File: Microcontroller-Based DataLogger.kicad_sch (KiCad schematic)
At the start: 25 parts, among them U1 24LC1025, U2 24LC1025, U3 DS1337S+, U4 ATMEGA328P-AN, Y1 Crystal, Y2 Crystal

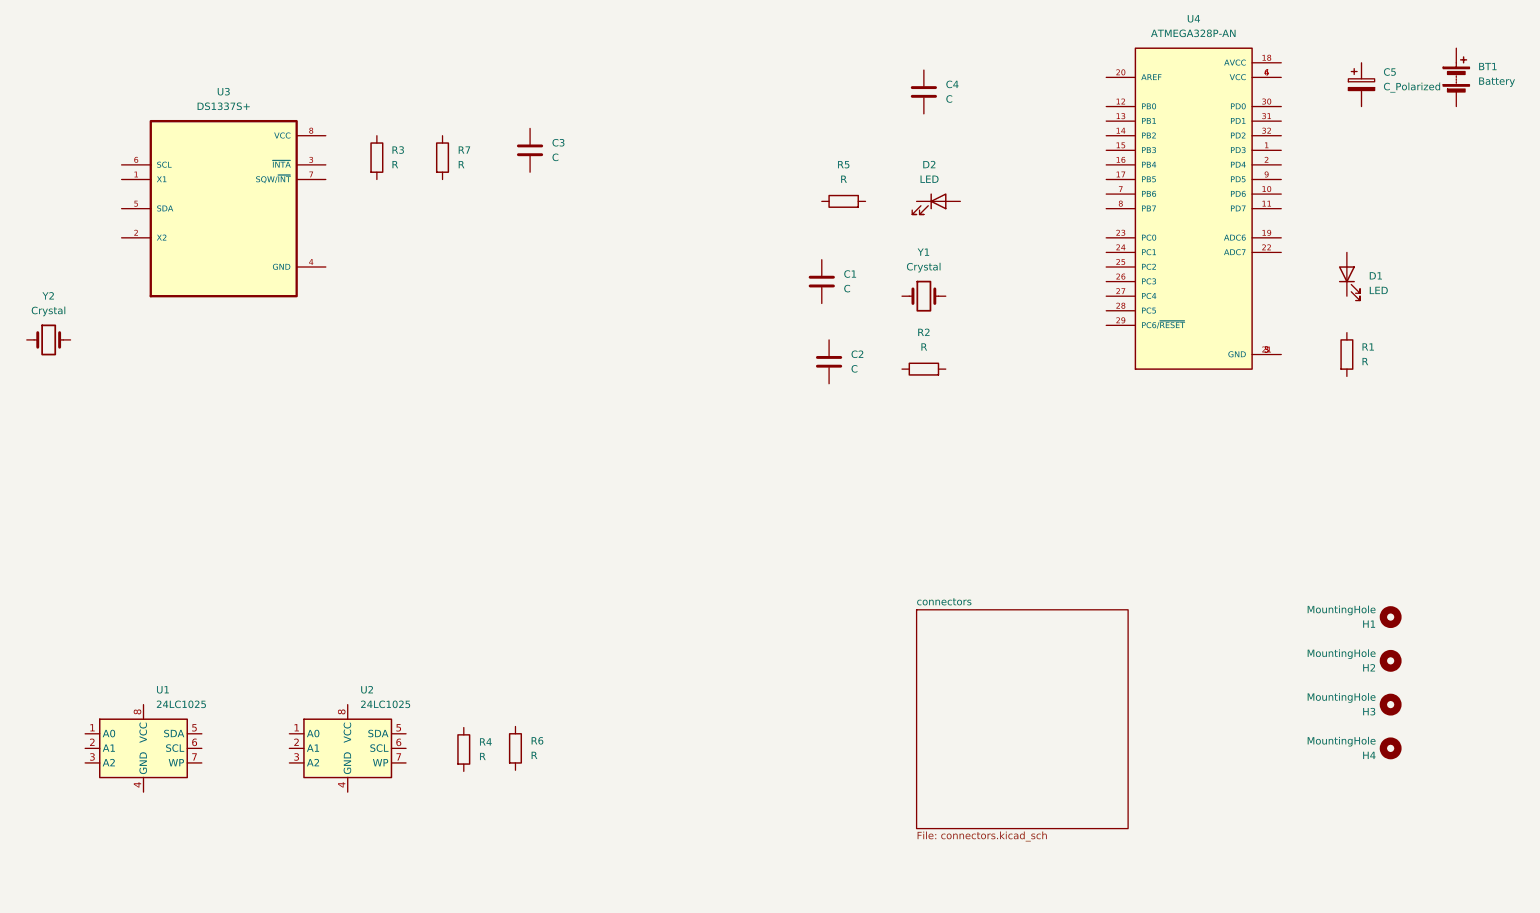
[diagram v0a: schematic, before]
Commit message: Completed symbol footprints.
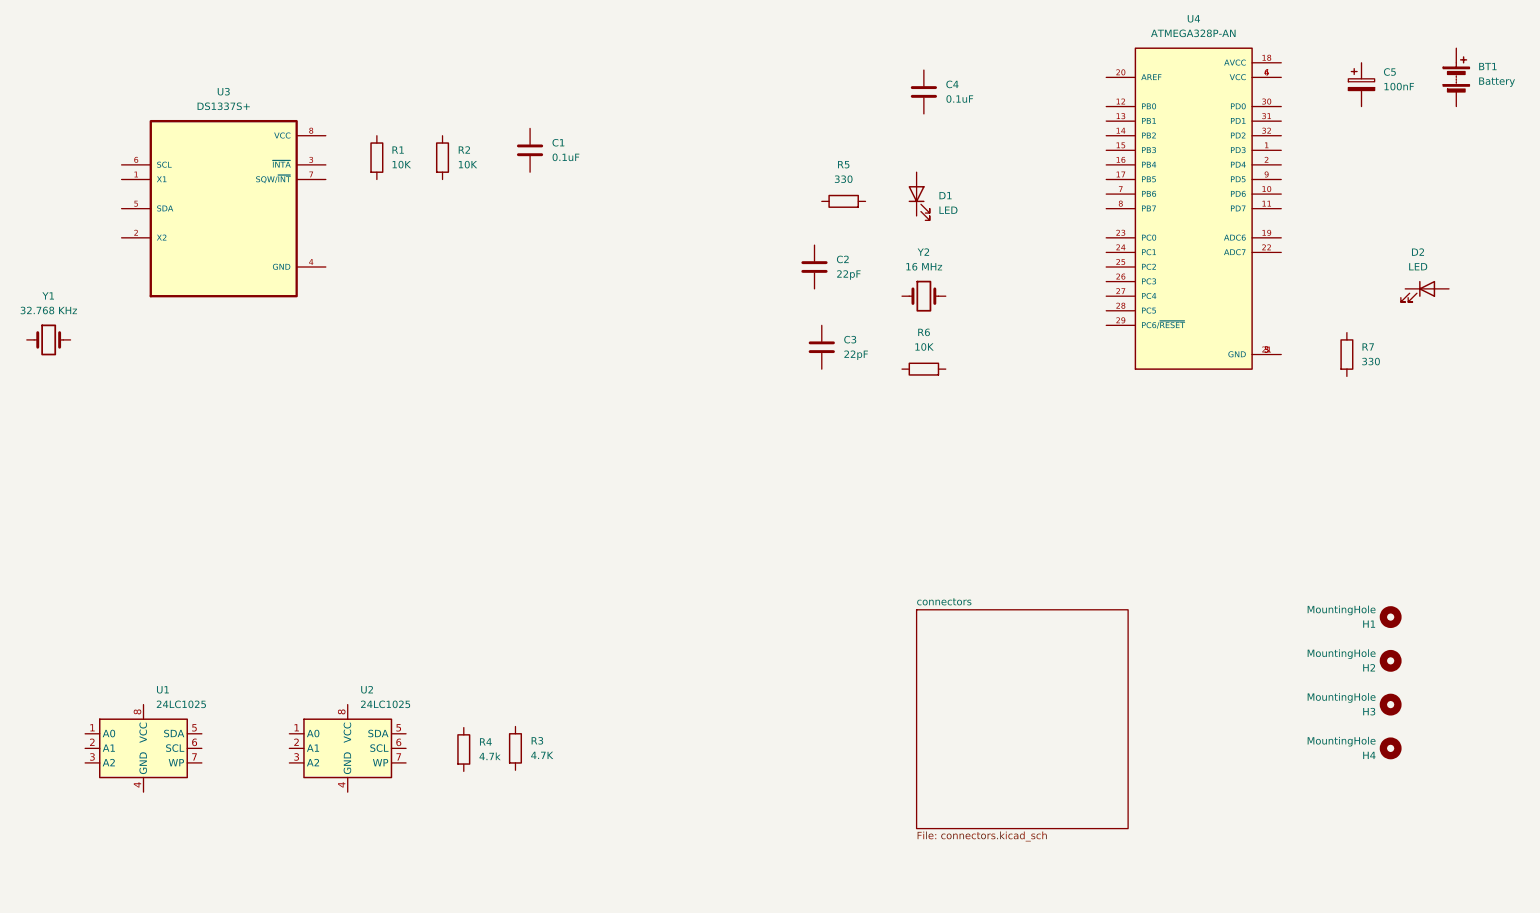
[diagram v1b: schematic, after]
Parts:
- BT1: footprint (none) -> Connector_PinHeader_2.54mm:PinHeader_1x02_P2.54mm_Vertical
- C1: renamed from C3; value C -> 0.1uF; footprint (none) -> Capacitor_SMD:C_0805_2012Metric
- C2: value C -> 22pF; footprint (none) -> Capacitor_SMD:C_0805_2012Metric
- C3: renamed from C1; value C -> 22pF; footprint (none) -> Capacitor_SMD:C_0805_2012Metric
- C4: value C -> 0.1uF; footprint (none) -> Capacitor_SMD:C_0805_2012Metric
- C5: value C_Polarized -> 100nF; footprint (none) -> Capacitor_SMD:C_0805_2012Metric
- D1, D2: footprint (none) -> LED_SMD:LED_0805_2012Metric
- H1, H2, H3, H4: footprint (none) -> MountingHole:MountingHole_2.1mm
- R1: renamed from R3; value R -> 10K; footprint (none) -> Resistor_SMD:R_0805_2012Metric
- R2: renamed from R7; value R -> 10K; footprint (none) -> Resistor_SMD:R_0805_2012Metric
- R3: renamed from R6; value R -> 4.7K; footprint (none) -> Resistor_SMD:R_0805_2012Metric
- R4: value R -> 4.7k; footprint (none) -> Resistor_SMD:R_0805_2012Metric
- R5: value R -> 330; footprint (none) -> Resistor_SMD:R_0805_2012Metric
- R6: renamed from R2; value R -> 10K; footprint (none) -> Resistor_SMD:R_0805_2012Metric
- R7: renamed from R1; value R -> 330; footprint (none) -> Resistor_SMD:R_0805_2012Metric
- U1, U2: footprint (none) -> Package_SO:SOIC-8_5.23x5.23mm_P1.27mm
- U3: footprint SOIC127P600X175-8N -> Footprints:SOIC127P600X175-8N
- U4: footprint QFP80P900X900X120-32N -> Footprints:QFP80P900X900X120-32N
- Y1: renamed from Y2; value Crystal -> 32.768 KHz; footprint (none) -> Crystal:Crystal_SMD_Abracon_ABM3-2Pin_5.0x3.2mm_HandSoldering
- Y2: renamed from Y1; value Crystal -> 16 MHz; footprint (none) -> Crystal:Crystal_SMD_Abracon_ABM3-2Pin_5.0x3.2mm_HandSoldering
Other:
- moved on the sheet: C2, C3, D1, D2

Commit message: complete wiring in 2nd page.
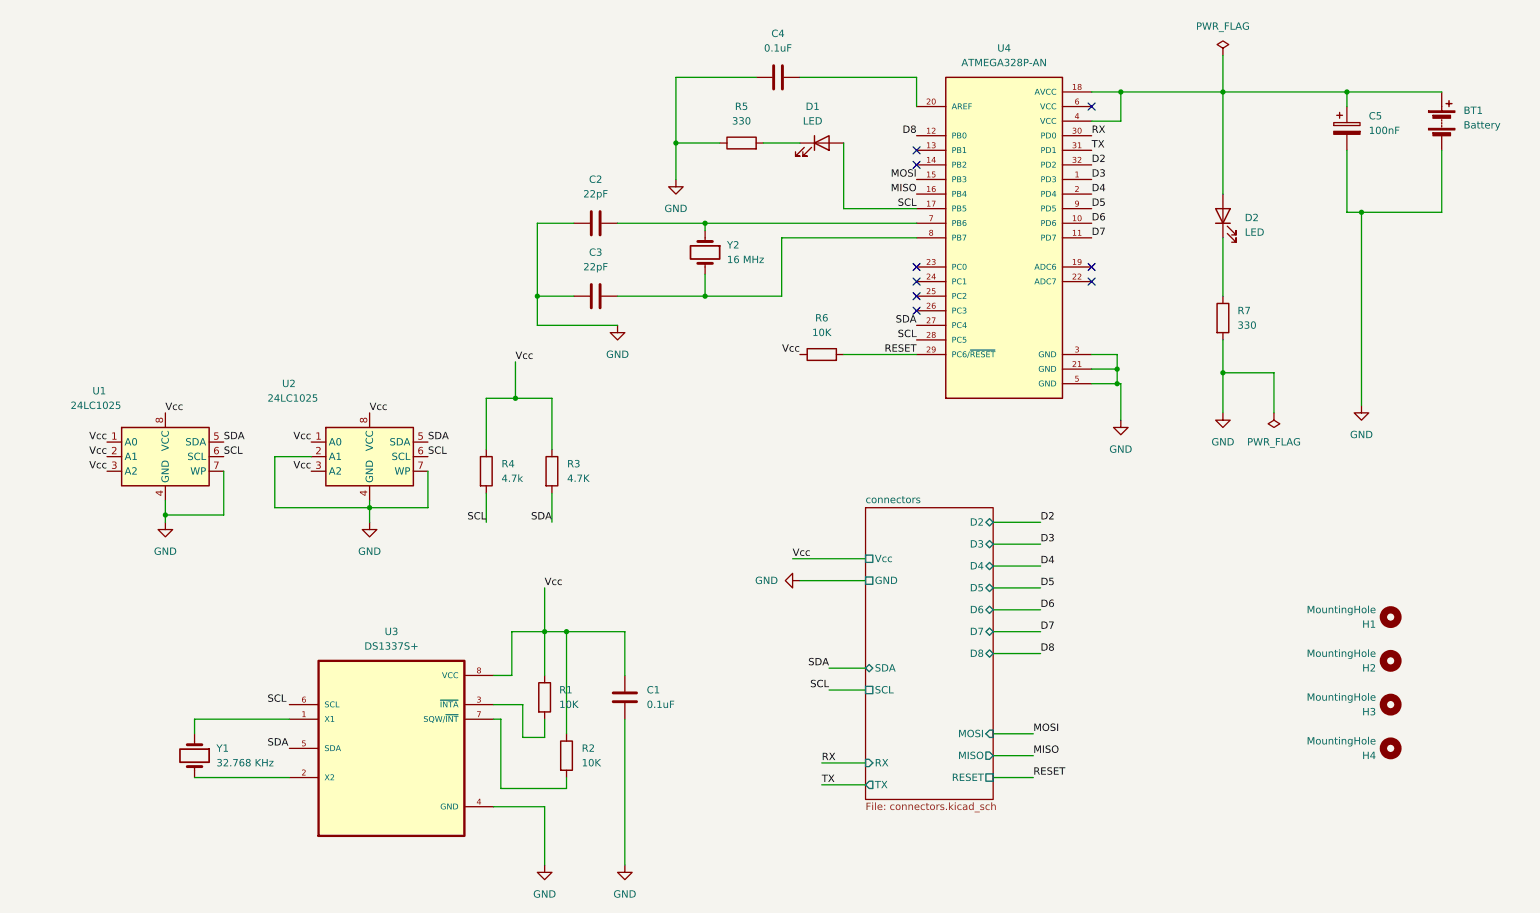
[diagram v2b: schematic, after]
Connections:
- net at D2.1 (K): now also R7.1
- net at D2.2 (A): now also BT1.1 (+), C5.1, U4.18 (AVCC), U4.4 (VCC)
- net at D1.1 (K): now also R5.2
- net SCL: now reaches D1.2 (A)
- net SCL: now also R4.2, U1.6 (SCL), U2.6 (SCL), U4.17 (PB5), U4.28 (PC5)
- net GND: now reaches BT1.2 (-)
- net GND: now also C1.2, C2.1, C3.2, C4.1, C5.2, R5.1, R7.2, U1.4 (GND), U1.7 (WP), U2.2 (A1), U2.4 (GND), U2.7 (WP), U3.4 (GND), U4.21 (GND), U4.3 (GND), U4.5 (GND)
- net Vcc: now reaches R6.1
- net Vcc: now also C1.1, R1.1, R2.1, R3.1, R4.1, U1.1 (A0), U1.2 (A1), U1.3 (A2), U1.8 (VCC), U2.1 (A0), U2.3 (A2), U2.8 (VCC), U3.8 (VCC)
- net RESET: now reaches R6.2
- net RESET: now also U4.29 (PC6/~{RESET})
- net D3: now reaches U4.1 (PD3)
- net D6: now reaches U4.10 (PD6)
- net D7: now reaches U4.11 (PD7)
- net D8: now reaches U4.12 (PB0)
- net MOSI: now reaches U4.15 (PB3)
- net MISO: now reaches U4.16 (PB4)
- net D4: now reaches U4.2 (PD4)
- net at U4.20 (AREF): now also C4.2
- net SDA: now reaches U4.27 (PC4)
- net SDA: now also R3.2, U1.5 (SDA), U2.5 (SDA)
- net RX: now reaches U4.30 (PD0)
- net TX: now reaches U4.31 (PD1)
- net D2: now reaches U4.32 (PD2)
- net at U4.6 (VCC): no longer U4.4 (VCC)
- net at U4.7 (PB6): now also C2.2, Y2.1
- net at U4.8 (PB7): now also C3.1, Y2.2
- net D5: now reaches U4.9 (PD5)
- net at U3.1 (X1): now also Y1.1
- net at U3.2 (X2): now also Y1.2
- net at U3.3 (~{INTA}): now also R1.2
- net at U3.7 (SQW/~{INT}): now also R2.2
- no-connect marks 0 -> 9
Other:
- sheet connectors ports: added D2, D3, D4, D5, D6, D7, D8, GND, MISO, MOSI, RESET, RX, SCL, SDA, TX, Vcc; removed none
- moved on the sheet: BT1, C1, C2, C3, C4, C5, D1, D2, R1, R2, R3, R4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

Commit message: complete 2nd page update wiring.
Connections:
- net SCL: now also U3.6 (SCL)
- net SDA: now also U3.5 (SDA)
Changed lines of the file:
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@@
 	)
 	(junction
+		(at 125.73 125.73)
+		(diameter 0)
+		(color 0 0 0 0)
+	)
+	(junction
 		(at 135.89 40.64)
 		(diameter 0)
@@
 	(wire
 		(pts
+			(xy 125.73 120.65) (xy 125.73 125.73)
+		)
+		(stroke
+			(width 0)
+			(type default)
+		)
+	)
+	(wire
+		(pts
 			(xy 104.14 156.21) (xy 113.03 156.21)
 		)
@@
 	(wire
 		(pts
+			(xy 64.77 138.43) (xy 68.58 138.43)
+		)
+		(stroke
+			(width 0)
+			(type default)
+		)
+	)
+	(wire
+		(pts
 			(xy 213.36 36.83) (xy 213.36 31.75)
 		)
@@
 	(wire
 		(pts
-			(xy 116.84 125.73) (xy 127 125.73)
+			(xy 116.84 125.73) (xy 125.73 125.73)
 		)
 		(stroke
@@
 	(wire
 		(pts
+			(xy 125.73 125.73) (xy 127 125.73)
+		)
+		(stroke
+			(width 0)
+			(type default)
+		)
+	)
+	(wire
+		(pts
 			(xy 255.27 52.705) (xy 255.27 86.36)
 		)
@@
 	(wire
 		(pts
+			(xy 64.77 146.05) (xy 68.58 146.05)
+		)
+		(stroke
+			(width 0)
+			(type default)
+		)
+	)
+	(wire
+		(pts
 			(xy 231.14 87.63) (xy 231.14 80.645)
 		)
@@
 		)
 	)
-	(label "Vcc"
-		(at 46.99 87.63 0)
-		(fields_autoplaced yes)
-		(effects
-			(font
-				(size 1.27 1.27)
-			)
-			(justify left bottom)
-		)
-	)
 	(label "MOSI"
 		(at 177.8 46.99 180)
@@
 	)
 	(label "Vcc"
+		(at 46.99 87.63 0)
+		(fields_autoplaced yes)
+		(effects
+			(font
+				(size 1.27 1.27)
+			)
+			(justify left bottom)
+		)
+	)
+	(label "Vcc"
 		(at 36.83 95.25 180)
 		(fields_autoplaced yes)
@@
 					(unit 1)
 				)
+			)
+		)
+	)
+	(symbol
+		(lib_id "power:PWR_FLAG")
+		(at 125.73 120.65 0)
+		(unit 1)
+		(exclude_from_sim no)
+		(in_bom yes)
+		(on_board yes)
+		(dnp no)
+		(fields_autoplaced yes)
+		(property "Reference" "#FLG03"
+			(at 125.73 118.745 0)
+			(effects
+				(font
+					(size 1.27 1.27)
+				)
+				(hide yes)
+			)
+		)
+		(property "Value" "PWR_FLAG"
+			(at 125.73 115.57 0)
+			(effects
+				(font
+					(size 1.27 1.27)
+				)
+			)
+		)
+		(property "Footprint" ""
+			(at 125.73 120.65 0)
+			(effects
+				(font
+					(size 1.27 1.27)
+				)
+				(hide yes)
+			)
+		)
+		(property "Datasheet" "~"
+			(at 125.73 120.65 0)
+			(effects
+				(font
+					(size 1.27 1.27)
+				)
+				(hide yes)
+			)
+		)
+		(property "Description" "Special symbol for telling ERC where power comes from"
+			(at 125.73 120.65 0)
+			(effects
+				(font
+					(size 1.27 1.27)
+				)
+				(hide yes)
+			)
+		)
+		(pin "1"
+		)
+		(instances
+			(project ""
+				(path "/2f635a3b-74e6-4780-acb9-377dc19d282c"
+					(reference "#FLG03")
+					(unit 1)
+				)
